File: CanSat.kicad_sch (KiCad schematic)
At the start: 46 parts, among them IC1 W25Q128JVPIQ, J1 USB_C_Receptacle, J2 Conn_Coaxial, M1 SG-90, SW1 SW_Push, SW2 SW_Push, U1 MPU-6050, U4 RFM98W-433S2, U6 LM1085-5.0, U7 LM1085-3.3, U8 BMP280, U9 APS6404L-3SQR-ZR

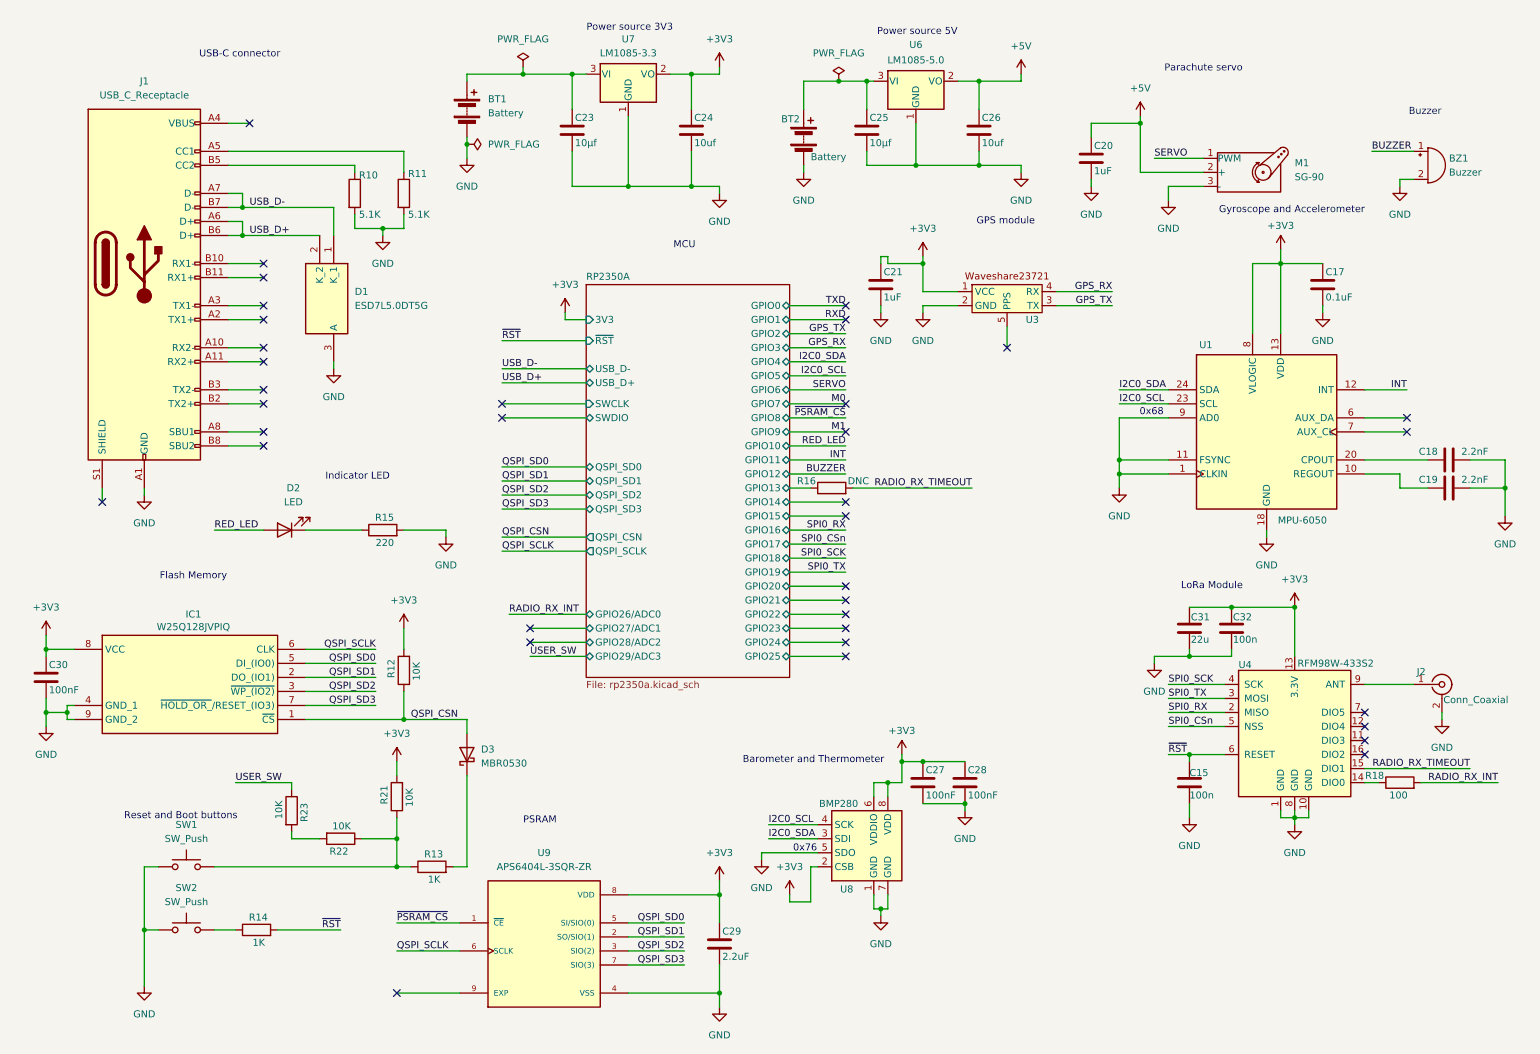
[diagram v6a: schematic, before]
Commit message: Added pin headers, debug headers, changed power source
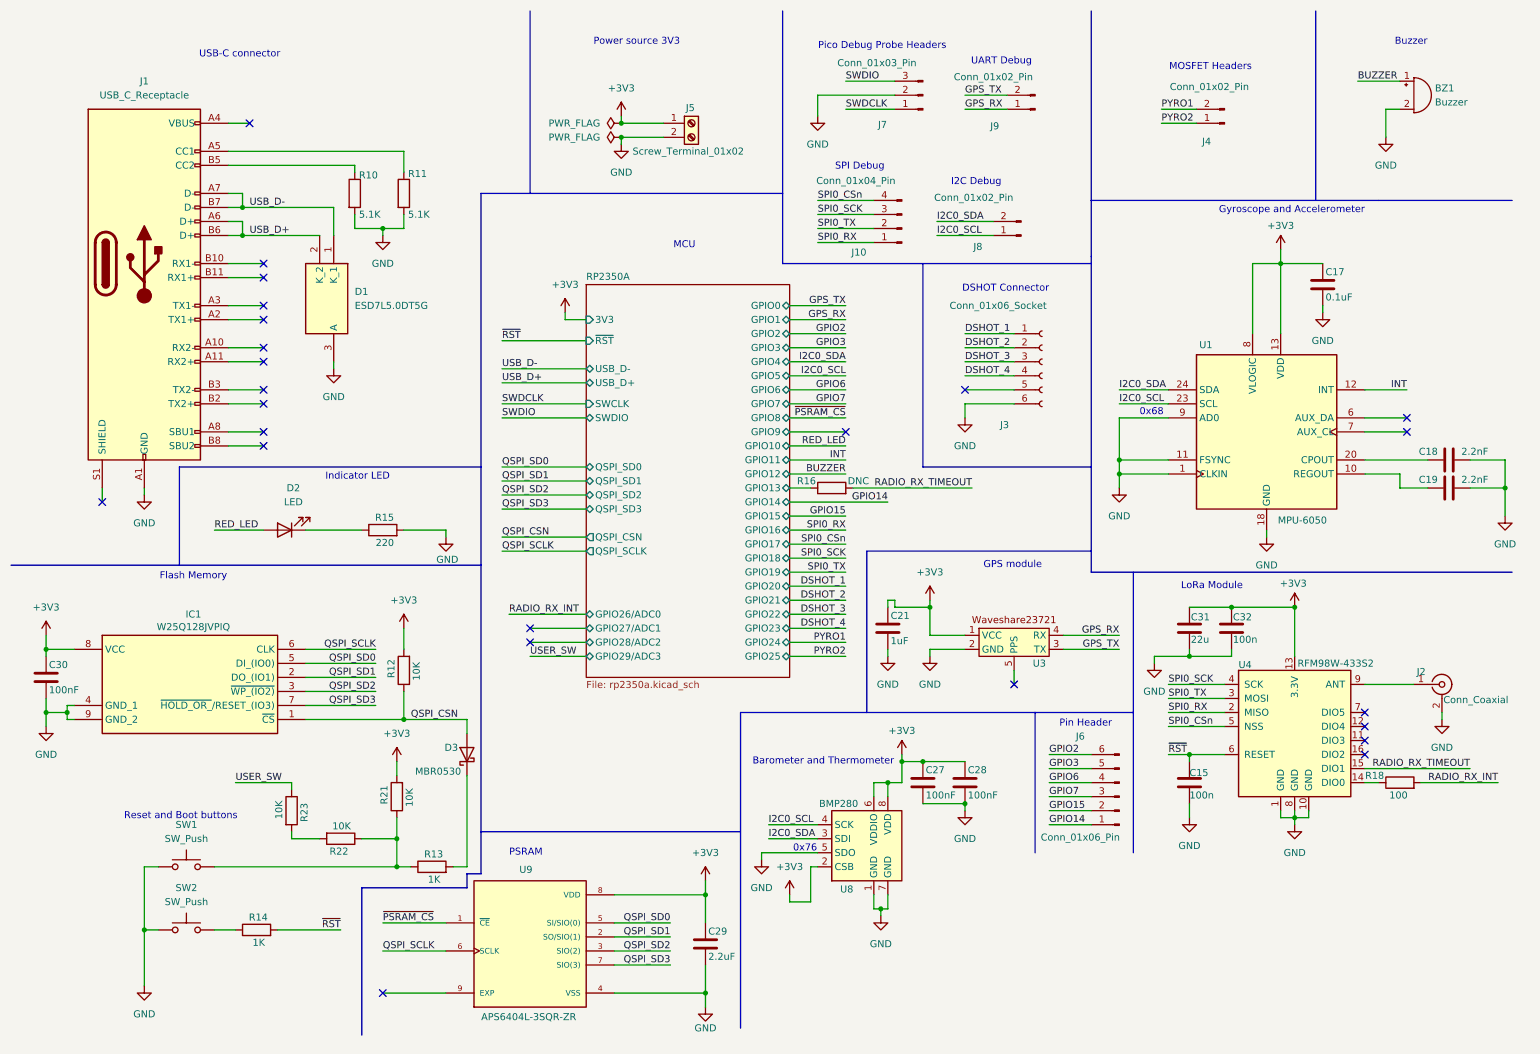
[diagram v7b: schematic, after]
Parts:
- removed BT1, BT2: Battery, Connector_PinHeader_1.00mm:PinHeader_1x02_P1.00mm_Vertical, symbol Device:Battery
- removed C20: 1uF, Capacitor_Tantalum_SMD:CP_EIA-2012-15_AVX-P, symbol Device:C
- removed C23, C25: 10µf, Capacitor_Tantalum_SMD:CP_EIA-2012-15_AVX-P, symbol Device:C
- removed C24, C26: 10uf, Capacitor_Tantalum_SMD:CP_EIA-2012-15_AVX-P, symbol Device:C
- removed M1: SG-90, Connector_PinHeader_1.00mm:PinHeader_1x03_P1.00mm_Vertical, symbol Motor:Motor_Servo
- removed U6: LM1085-5.0, LM1085IT-5.0:TO254P1054X470X1955-3, symbol Regulator_Linear:LM1085-5.0
- removed U7: LM1085-3.3, LM1085IT-3.3:TO254P1054X470X1955-3, symbol Regulator_Linear:LM1085-3.3
- added J10: Conn_01x04_Pin, Connector_PinHeader_1.00mm:PinHeader_1x04_P1.00mm_Vertical, symbol Connector:Conn_01x04_Pin
- added J3: Conn_01x06_Socket, Connector_JST:JST_SH_BM06B-SRSS-TB_1x06-1MP_P1.00mm_Vertical, symbol Connector:Conn_01x06_Socket
- added J4, J8, J9: Conn_01x02_Pin, Connector_PinHeader_1.00mm:PinHeader_1x02_P1.00mm_Vertical, symbol Connector:Conn_01x02_Pin
- added J5: Screw_Terminal_01x02, TerminalBlock:TerminalBlock_bornier-2_P5.08mm, symbol Connector:Screw_Terminal_01x02
- added J6: Conn_01x06_Pin, Connector_PinHeader_1.00mm:PinHeader_2x03_P1.00mm_Vertical, symbol Connector:Conn_01x06_Pin
- added J7: Conn_01x03_Pin, Connector_PinHeader_1.00mm:PinHeader_1x03_P1.00mm_Vertical, symbol Connector:Conn_01x03_Pin
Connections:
- net +3V3: now also J5.1 (Pin_1)
- net GND: now also J3.6 (Pin_6), J5.2 (Pin_2), J7.2 (Pin_2)
- net GPS_RX: now also J9.1 (Pin_1)
- net GPS_TX: now also J9.2 (Pin_2)
- net I2C0_SCL: now also J8.1 (Pin_1)
- net I2C0_SDA: now also J8.2 (Pin_2)
- net SPI0_CSn: now also J10.4 (Pin_4)
- net SPI0_RX: now also J10.1 (Pin_1)
- net SPI0_SCK: now also J10.3 (Pin_3)
- net SPI0_TX: now also J10.2 (Pin_2)
- new net DSHOT_1: J3.1 (Pin_1)
- new net DSHOT_2: J3.2 (Pin_2)
- new net DSHOT_3: J3.3 (Pin_3)
- new net DSHOT_4: J3.4 (Pin_4)
- new net GPIO14: J6.1 (Pin_1)
- new net GPIO15: J6.2 (Pin_2)
- new net GPIO2: J6.6 (Pin_6)
- new net GPIO3: J6.5 (Pin_5)
- new net GPIO6: J6.4 (Pin_4)
- new net GPIO7: J6.3 (Pin_3)
- new net PYRO1: J4.2 (Pin_2)
- new net PYRO2: J4.1 (Pin_1)
- new net SWDCLK: J7.1 (Pin_1)
- new net SWDIO: J7.3 (Pin_3)
- no-connect marks 36 -> 24
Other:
- note added: "DSHOT Connector"
- note added: "I2C Debug"
- note added: "MOSFET Headers"
- note added: "Pico Debug Probe Headers"
- note added: "Pin Header"
- note added: "SPI Debug"
- note added: "UART Debug"
- note removed: "Parachute servo"
- note removed: "Power source 5V"
- moved on the sheet: BZ1, C21, C29, U3, U9

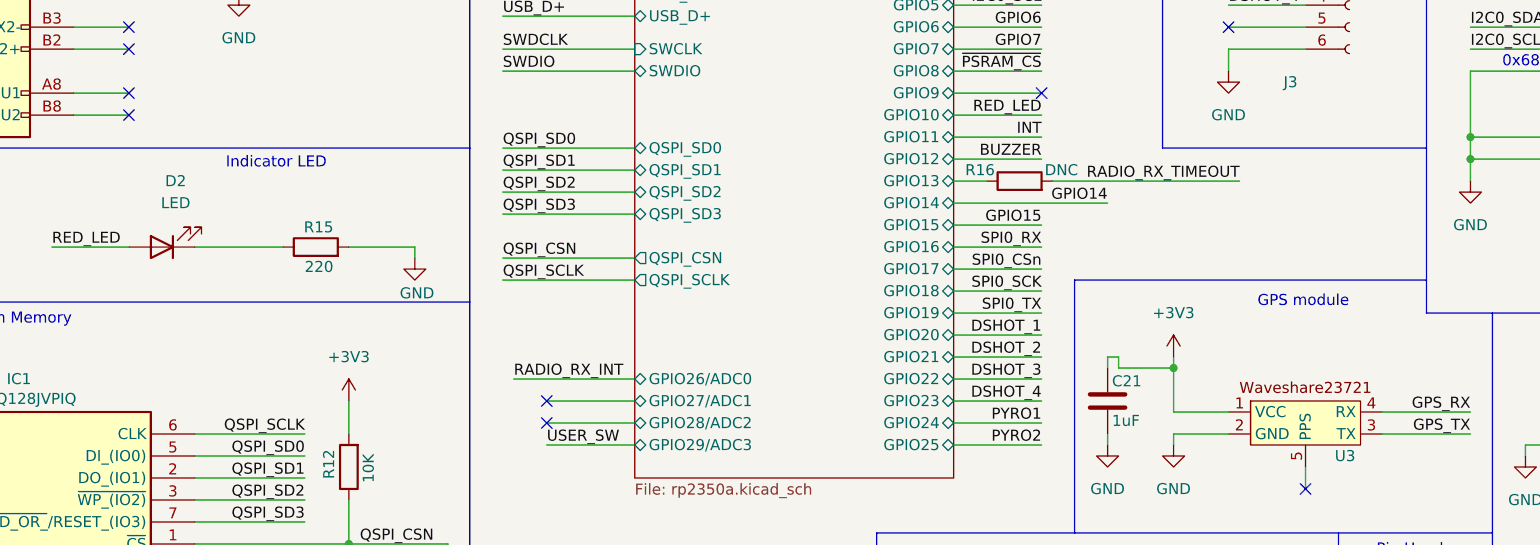
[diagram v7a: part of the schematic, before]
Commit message: Added BOM to readme
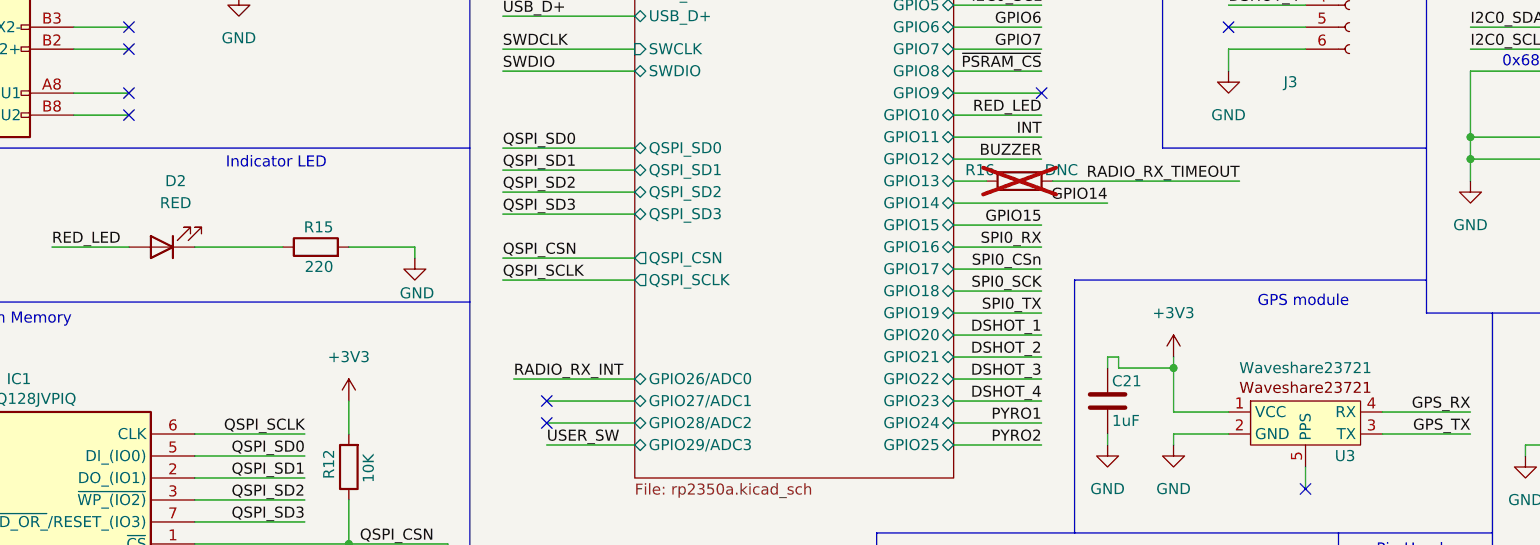
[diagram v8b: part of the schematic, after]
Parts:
- D2: value LED -> RED
- R16: now not fitted
- U3: value ~ -> Waveshare23721
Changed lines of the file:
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@@
 			)
 		)
-		(property "Value" "LED"
+		(property "Value" "RED"
 			(at 63.8175 101.6 0)
 			(effects
@@
 		(in_bom yes)
 		(on_board yes)
-		(dnp no)
+		(dnp yes)
 		(property "Reference" "R16"
 			(at 156.718 97.79 90)
@@
 			)
 		)
-		(property "Value" "~"
+		(property "Value" "Waveshare23721"
 			(at 194.31 120.65 0)
 			(effects
